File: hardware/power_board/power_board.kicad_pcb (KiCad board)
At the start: 2 copper layers, 97.2 x 72.6 mm, 32 parts, among them J1 MCU, J2 MAINS_IN, J8 HEATER, K1 BOOST, K2 OFFPEAK, Q1 MMBT3904, Q2 MMBT3904, Q3 MMBT3904, U1 PC817, U2 PC817, U3 AMS1117-3.3

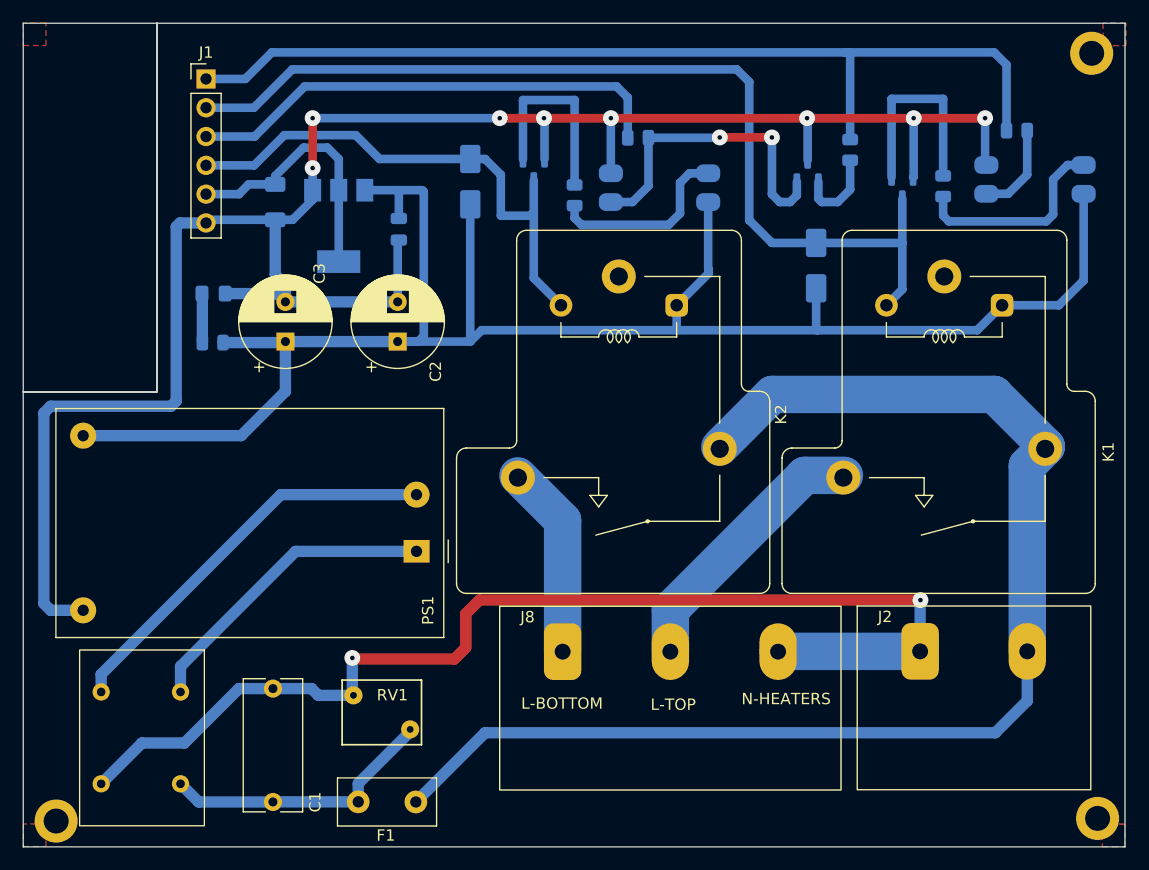
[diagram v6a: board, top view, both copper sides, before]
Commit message: fix boards so they components are on the correct side lol
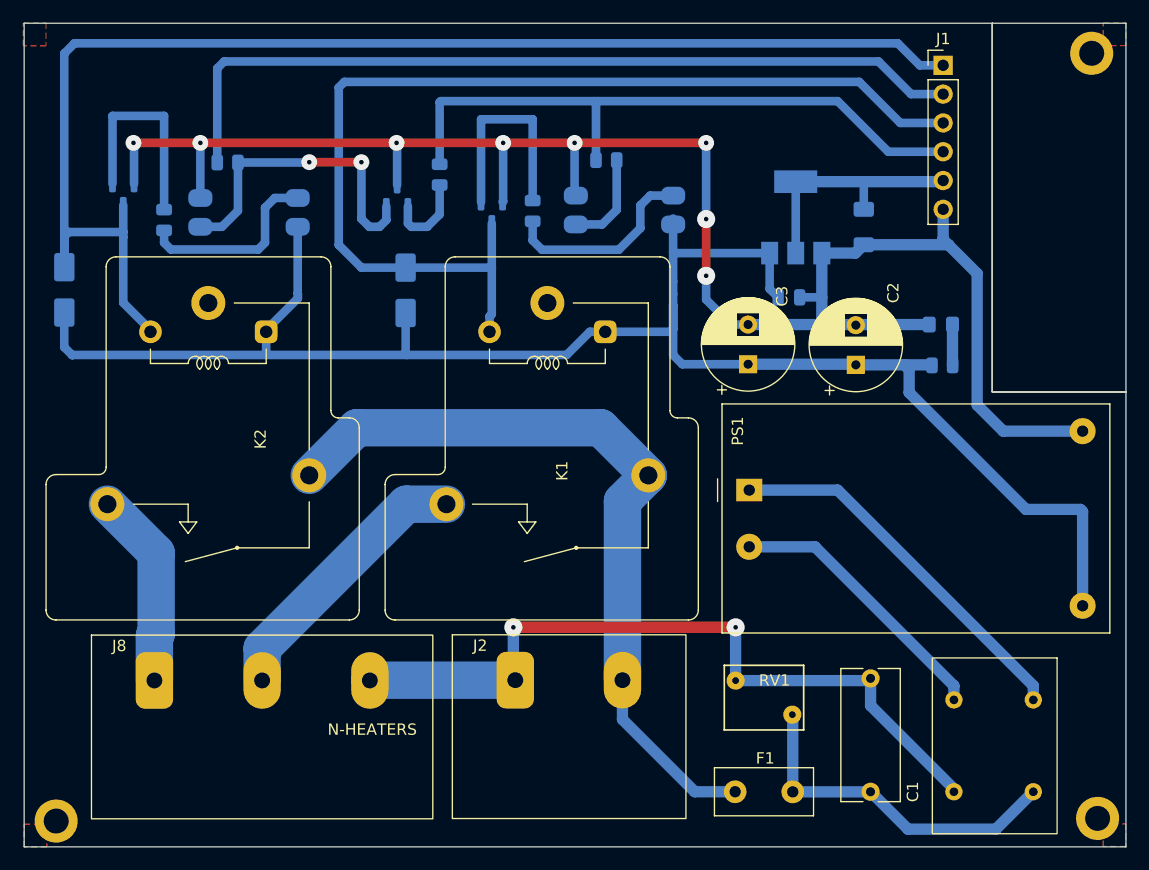
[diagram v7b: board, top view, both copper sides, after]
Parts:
- moved L1 75.2 mm to (186.2, 118.6)
- moved J1 65.0 mm to (176.1, 66.3)
- moved R8 64.4 mm to (176.0, 92.8), turned to 0 degrees
- moved D3 64.2 mm to (175.9, 89.2), turned to 0 degrees
- moved C1 52.7 mm to (169.7, 130.4)
- moved C5 51.9 mm to (169.1, 80.6)
- moved C3 40.8 mm to (158.9, 92.7)
- moved C2 40.5 mm to (168.4, 92.8)
- moved U3 40.3 mm to (163.1, 79.8), turned to 90 degrees
- moved D2 37.0 mm to (98.6, 86.1)
- moved U1 36.3 mm to (148.0, 79.1)
- moved R1 36.3 mm to (146.4, 74.7)
- moved K2 36.3 mm to (111.3, 87.3)
- moved D1 36.3 mm to (128.7, 86.2)
- moved R2 36.3 mm to (131.7, 76.0)
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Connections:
- J1 pad 1: RELAY_BOOST -> LED_OFFPEAK
- J1 pad 2: LED_BOOST -> RELAY_OFFPEAK
- J1 pad 3: RELAY_OFFPEAK -> LED_BOOST
- J1 pad 4: LED_OFFPEAK -> RELAY_BOOST
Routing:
- net LED_OFFPEAK: track 47.2 -> 117.6 mm
- net MAINSIN_L: track 113.4 -> 68.4 mm
- net MAINSIN_N: track 100.4 -> 66.9 mm
- net RELAY_OFFPEAK: track 43.0 -> 73.8 mm
- net RELAY_BOOST: track 85.5 -> 57.0 mm
- net GND: track 177.8 -> 155.3 mm
- net Net-(PS1-AC/N): track 35.9 -> 24.4 mm
- net LED_BOOST: track 86.6 -> 92.9 mm
- net Net-(PS1-AC/L): track 27.3 -> 33.4 mm
- net Net-(C1-Pad1): track 24.6 -> 30.8 mm
- net +5V: track 161.0 -> 154.9 mm
- net Net-(Q3-B): track 17.5 -> 19.1 mm
- net +3.3V: track 23.5 -> 22.2 mm
- net Net-(Q2-B): track 18.3 -> 19.0 mm
- net Net-(D3-A): track 4.34 -> 3.61 mm
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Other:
- outline, holes or cut-outs redrawn
- board text removed: "L-BOTTOM"
- board text removed: "L-TOP"

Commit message: move screw position
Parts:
- moved ? 91.8 mm to (97.4, 65.5)
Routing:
- net LED_OFFPEAK: track 117.6 -> 113.8 mm
- net MAINSIN_N: track 66.9 -> 66.0 mm
- added copper zone on B.Cu, net (none)
- removed copper zone on F.Cu, net (none)
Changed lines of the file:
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@@
     (pcbplotparams
       (layerselection 0x0001000_7ffffffe)
-      (plot_on_all_layers_selection 0x003f030_00000000)
+      (plot_on_all_layers_selection 0x003ff30_80000001)
       (disableapertmacros false)
       (usegerberextensions false)
@@
       (dxfimperialunits false)
       (dxfusepcbnewfont true)
-      (psnegative true)
+      (psnegative false)
       (psa4output false)
       (plotreference false)
@@
     )
   )
+  (footprint "" (layer "F.Cu")
+    (at 97.362499 65.512651)
+    (fp_text reference "" (at 0 0) (layer "F.SilkS")
+        (effects (font (size 1.27 1.27) (thickness 0.15)))
+    )
+    (fp_text value "" (at 0 0) (layer "F.SilkS")
+        (effects (font (size 1.27 1.27) (thickness 0.15)))
+    )
+    (pad "1" thru_hole circle (at 0 0 180) (size 3.8 3.8) (drill 2.2) (layers "*.Cu" "*.Mask"))
+  )
   (footprint "Converter_ACDC:Converter_ACDC_HiLink_HLK-PMxx" (layer "F.Cu")
     (at 159 103.8)
@@
       (rotate (xyz 0 0 0))
     )
-  )
-  (footprint "" locked (layer "F.Cu")
-    (at 189.199848 65.28)
-    (fp_text reference "" (at 0 0) (layer "F.SilkS")
-        (effects (font (size 1.27 1.27) (thickness 0.15)))
-    )
-    (fp_text value "" (at 0 0) (layer "F.SilkS")
-        (effects (font (size 1.27 1.27) (thickness 0.15)))
-    )
-    (pad "1" thru_hole circle locked (at 0 0 180) (size 3.8 3.8) (drill 2.2) (layers "*.Cu" "*.Mask"))
   )
   (footprint "TerminalBlock2:HB9500-9.5-3P" (layer "F.Cu")
@@
   (gr_line locked (start 180.43 62.63) (end 95.06 62.63)
     (stroke (width 0.1) (type default)) (layer "Edge.Cuts"))
-  (gr_rect locked (start 192.22 62.63) (end 180.43 95.14)
+  (gr_rect locked (start 180.43 62.63) (end 192.22 95.14)
     (stroke (width 0.1) (type default)) (fill none) (layer "Edge.Cuts"))
   (gr_line locked (start 192.22 135.26) (end 192.22 95.14)
@@
   (segment (start 116.4 89.68) (end 119.2 86.88) (width 0.76) (layer "B.Cu") (net 4))
   (segment (start 119.18 86.46) (end 119.18 80.58) (width 0.76) (layer "B.Cu") (net 4))
-  (segment (start 157.8 115.9) (end 138.2 115.9) (width 1) (layer "F.Cu") (net 5))
+  (segment (start 154.46 115.9) (end 138.2 115.9) (width 1) (layer "F.Cu") (net 5))
+  (segment (start 157.8 117.47) (end 156.03 117.47) (width 1) (layer "F.Cu") (net 5))
+  (segment (start 156.03 117.47) (end 154.46 115.9) (width 1) (layer "F.Cu") (net 5))
   (via (at 138.2 115.9) (size 1.6) (drill 0.4) (layers "F.Cu" "B.Cu") (net 5))
-  (via (at 157.8 115.9) (size 1.6) (drill 0.4) (layers "F.Cu" "B.Cu") (net 5))
+  (via (at 157.8 117.47) (size 1.6) (drill 0.4) (layers "F.Cu" "B.Cu") (net 5))
   (segment (start 157.8 120.6) (end 169.5 120.6) (width 1) (layer "B.Cu") (net 5))
   (segment (start 177.05 130.4) (end 177.05 130.15) (width 1) (layer "B.Cu") (net 5))
@@
   (segment (start 177.05 130.15) (end 169.7 122.8) (width 1) (layer "B.Cu") (net 5))
   (segment (start 138.2 120.39) (end 138.37 120.56) (width 1) (layer "B.Cu") (net 5))
-  (segment (start 157.8 120.6) (end 157.8 115.9) (width 1) (layer "B.Cu") (net 5))
   (segment (start 125.57 120.56) (end 125.545 120.585) (width 3.3) (layer "B.Cu") (net 5))
   (segment (start 138.37 120.56) (end 125.57 120.56) (width 3.3) (layer "B.Cu") (net 5))
+  (segment (start 157.8 120.6) (end 157.8 117.47) (width 1) (layer "B.Cu") (net 5))
   (segment (start 154.2 130.4) (end 147.82 124.02) (width 1) (layer "B.Cu") (net 6))
   (segment (start 145.9 98.3) (end 150.1 102.5) (width 3.3) (layer "B.Cu") (net 6))
@@
   (segment (start 103.8 81.48) (end 103.8 87.28) (width 0.76) (layer "B.Cu") (net 8))
   (segment (start 172.1 64.4) (end 174.04 66.34) (width 0.76) (layer "B.Cu") (net 8))
-  (segment (start 99.5 64.4) (end 172.1 64.4) (width 0.76) (layer "B.Cu") (net 8))
+  (segment (start 174.04 66.34) (end 176.1 66.34) (width 0.76) (layer "B.Cu") (net 8))
   (segment (start 103.8 81.48) (end 103.8 81.04) (width 0.76) (layer "B.Cu") (net 8))
   (segment (start 103.8 87.28) (end 106.2 89.68) (width 0.76) (layer "B.Cu") (net 8))
-  (segment (start 174.04 66.34) (end 176.1 66.34) (width 0.76) (layer "B.Cu") (net 8))
-  (segment (start 98.6 65.3) (end 99.5 64.4) (width 0.76) (layer "B.Cu") (net 8))
   (segment (start 99 81.04) (end 103.8 81.04) (width 0.76) (layer "B.Cu") (net 8))
+  (segment (start 106.02 64.4) (end 172.1 64.4) (width 0.76) (layer "B.Cu") (net 8))
   (segment (start 103.8 81.04) (end 103.8 78.68) (width 0.76) (layer "B.Cu") (net 8))
+  (segment (start 98.6 84.14) (end 98.6 71.82) (width 0.76) (layer "B.Cu") (net 8))
   (segment (start 98.6 84.14) (end 98.6 81.44) (width 0.76) (layer "B.Cu") (net 8))
   (segment (start 98.6 81.44) (end 99 81.04) (width 0.76) (layer "B.Cu") (net 8))
-  (segment (start 98.6 84.14) (end 98.6 65.3) (width 0.76) (layer "B.Cu") (net 8))
+  (segment (start 98.6 71.82) (end 106.02 64.4) (width 0.76) (layer "B.Cu") (net 8))
   (segment (start 170.4 66) (end 173.28 68.88) (width 0.76) (layer "B.Cu") (net 9))
   (segment (start 112.7 66) (end 112.0875 66.6125) (width 0.76) (layer "B.Cu") (net 9))
@@
   (segment (start 106.545 116.655) (end 106.545 120.585) (width 3.3) (layer "B.Cu") (net 24))
   (segment (start 106.7 116.5) (end 106.545 116.655) (width 3.3) (layer "B.Cu") (net 24))
-  (zone locked (net 0) (net_name "") (layer "F.Cu") (hatch edge 0.5)
+  (zone (net 0) (net_name "") (layer "B.Cu") (hatch edge 0.5)
     (connect_pads (clearance 0))
     (min_thickness 0.05) (filled_areas_thickness no)
@@
     (polygon
       (pts
-        (xy 190.21 135.23)
-        (xy 190.21 133.23)
-        (xy 192.21 133.23)
-        (xy 192.21 135.23)
+        (xy 97 135.23)
+        (xy 97 133.23)
+        (xy 95 133.23)
+        (xy 95 135.23)
       )
     )
   )
-  (zone locked (net 0) (net_name "") (layer "F.Cu") (hatch edge 0.5)
+  (zone (net 0) (net_name "") (layer "B.Cu") (hatch edge 0.5)
     (connect_pads (clearance 0))
     (min_thickness 0.05) (filled_areas_thickness no)
@@
     (polygon
       (pts
-        (xy 94.99 64.61)
-        (xy 94.99 62.61)
-        (xy 96.99 62.61)
-        (xy 96.99 64.61)
+        (xy 192.22 64.61)
+        (xy 192.22 62.61)
+        (xy 190.22 62.61)
+        (xy 190.22 64.61)
       )
     )
   )
-  (zone locked (net 0) (net_name "") (layer "F.Cu") (hatch edge 0.5)
+  (zone (net 0) (net_name "") (layer "B.Cu") (hatch edge 0.5)
     (connect_pads (clearance 0))
     (min_thickness 0.05) (filled_areas_thickness no)
@@
     (polygon
       (pts
-        (xy 190.22 64.6)
-        (xy 190.22 62.6)
-        (xy 192.22 62.6)
-        (xy 192.22 64.6)
+        (xy 96.99 64.6)
+        (xy 96.99 62.6)
+        (xy 94.99 62.6)
+        (xy 94.99 64.6)
       )
     )
   )
-  (zone locked (net 0) (net_name "") (layer "F.Cu") (hatch edge 0.5)
+  (zone (net 0) (net_name "") (layer "B.Cu") (hatch edge 0.5)
     (connect_pads (clearance 0))
     (min_thickness 0.05) (filled_areas_thickness no)
@@
     (polygon
       (pts
-        (xy 95.06 135.26)
-        (xy 95.06 133.26)
-        (xy 97.06 133.26)
-        (xy 97.06 135.26)
+        (xy 192.15 135.26)
+        (xy 192.15 133.26)
+        (xy 190.15 133.26)
+        (xy 190.15 135.26)
       )
     )
